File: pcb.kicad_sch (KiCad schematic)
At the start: 3 parts, among them SW1 SW_PUSH, U1 ProMicro

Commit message: rename repo and folder
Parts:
- added D10, D11, D12, D13, D14, D15, D16, D17, D18, D19, D2, D20, D21, D22, D23, D24, D25, D26, D27, D28, D29, D3, D30, D31, D32, D33, D34, D35, D36, D37, D38, D39, D4, D40, D41, D42, D5, D6, D7, D8, D9: 1N4148W, Diode_SMD:D_SOD-123, symbol Diode:1N4148W
- added SW10, SW11, SW12, SW13, SW14, SW15, SW16, SW17, SW18, SW2, SW20, SW21, SW22, SW23, SW24, SW25, SW26, SW27, SW28, SW29, SW3, SW30, SW31, SW32, SW33, SW34, SW35, SW36, SW37, SW38, SW39, SW4, SW40, SW41, SW42, SW43, SW5, SW6, SW7, SW8, SW9: SW_PUSH, symbol kbd:SW_PUSH
- added SW19: RESETSW, symbol kbd:SW_PUSH
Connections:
- net COL0: now also SW1.1, SW13.1, SW23.1, SW29.1, SW35.1, SW41.1, SW7.1
- net COL1: now also SW14.1, SW2.1, SW24.1, SW30.1, SW36.1, SW42.1, SW8.1
- net COL2: now also SW15.1, SW25.1, SW3.1, SW31.1, SW37.1, SW43.1, SW9.1
- net COL3: now also SW10.1, SW16.1, SW20.1, SW26.1, SW32.1, SW38.1, SW4.1
- net COL4: now also SW11.1, SW17.1, SW21.1, SW27.1, SW33.1, SW39.1, SW5.1
- net COL5: now also SW12.1, SW18.1, SW22.1, SW28.1, SW34.1, SW40.1, SW6.1
- net GND: now also SW19.2
- net ROW0: now also D1.1 (K), D2.1 (K), D3.1 (K), D4.1 (K), D5.1 (K), D6.1 (K)
- net ROW1: now also D10.1 (K), D11.1 (K), D12.1 (K), D7.1 (K), D8.1 (K), D9.1 (K)
- net ROW2: now also D13.1 (K), D14.1 (K), D15.1 (K), D16.1 (K), D17.1 (K), D18.1 (K)
- net ROW3: now also D19.1 (K), D20.1 (K), D21.1 (K)
- net ROW4: now also D22.1 (K), D23.1 (K), D24.1 (K), D25.1 (K), D26.1 (K), D27.1 (K)
- net ROW5: now also D28.1 (K), D29.1 (K), D30.1 (K), D31.1 (K), D32.1 (K), D33.1 (K)
- net ROW6: now also D34.1 (K), D35.1 (K), D36.1 (K), D37.1 (K), D38.1 (K), D39.1 (K)
- net ROW7: now also D40.1 (K), D41.1 (K), D42.1 (K)
- net at SW1.2: now also D1.2 (A)
- net at U1.22 (RST): now also SW19.1
- new net: D27.2 (A), SW28.2
- new net: D19.2 (A), SW20.2
- new net: D36.2 (A), SW37.2
- new net: D35.2 (A), SW36.2
- new net: D15.2 (A), SW15.2
- new net: D4.2 (A), SW4.2
- new net: D11.2 (A), SW11.2
- new net: D23.2 (A), SW24.2
- new net: D21.2 (A), SW22.2
- new net: D30.2 (A), SW31.2
- new net: D16.2 (A), SW16.2
- new net: D2.2 (A), SW2.2
- new net: D41.2 (A), SW42.2
- new net: D28.2 (A), SW29.2
- new net: D37.2 (A), SW38.2
- new net: D9.2 (A), SW9.2
- new net: D25.2 (A), SW26.2
- new net: D40.2 (A), SW41.2
- new net: D34.2 (A), SW35.2
- new net: D26.2 (A), SW27.2
- new net: D42.2 (A), SW43.2
- new net: D38.2 (A), SW39.2
- new net: D10.2 (A), SW10.2
- new net: D32.2 (A), SW33.2
- new net: D20.2 (A), SW21.2
- new net: D8.2 (A), SW8.2
- new net: D7.2 (A), SW7.2
- new net: D39.2 (A), SW40.2
- new net: D14.2 (A), SW14.2
- new net: D13.2 (A), SW13.2
- new net: D33.2 (A), SW34.2
- new net: D18.2 (A), SW18.2
- new net: D29.2 (A), SW30.2
- new net: D17.2 (A), SW17.2
- new net: D3.2 (A), SW3.2
- new net: D5.2 (A), SW5.2
- new net: D24.2 (A), SW25.2
- new net: D22.2 (A), SW23.2
- new net: D31.2 (A), SW32.2
- new net: D6.2 (A), SW6.2
- new net: D12.2 (A), SW12.2
- no-connect marks 0 -> 5
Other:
- moved on the sheet: D1, SW1

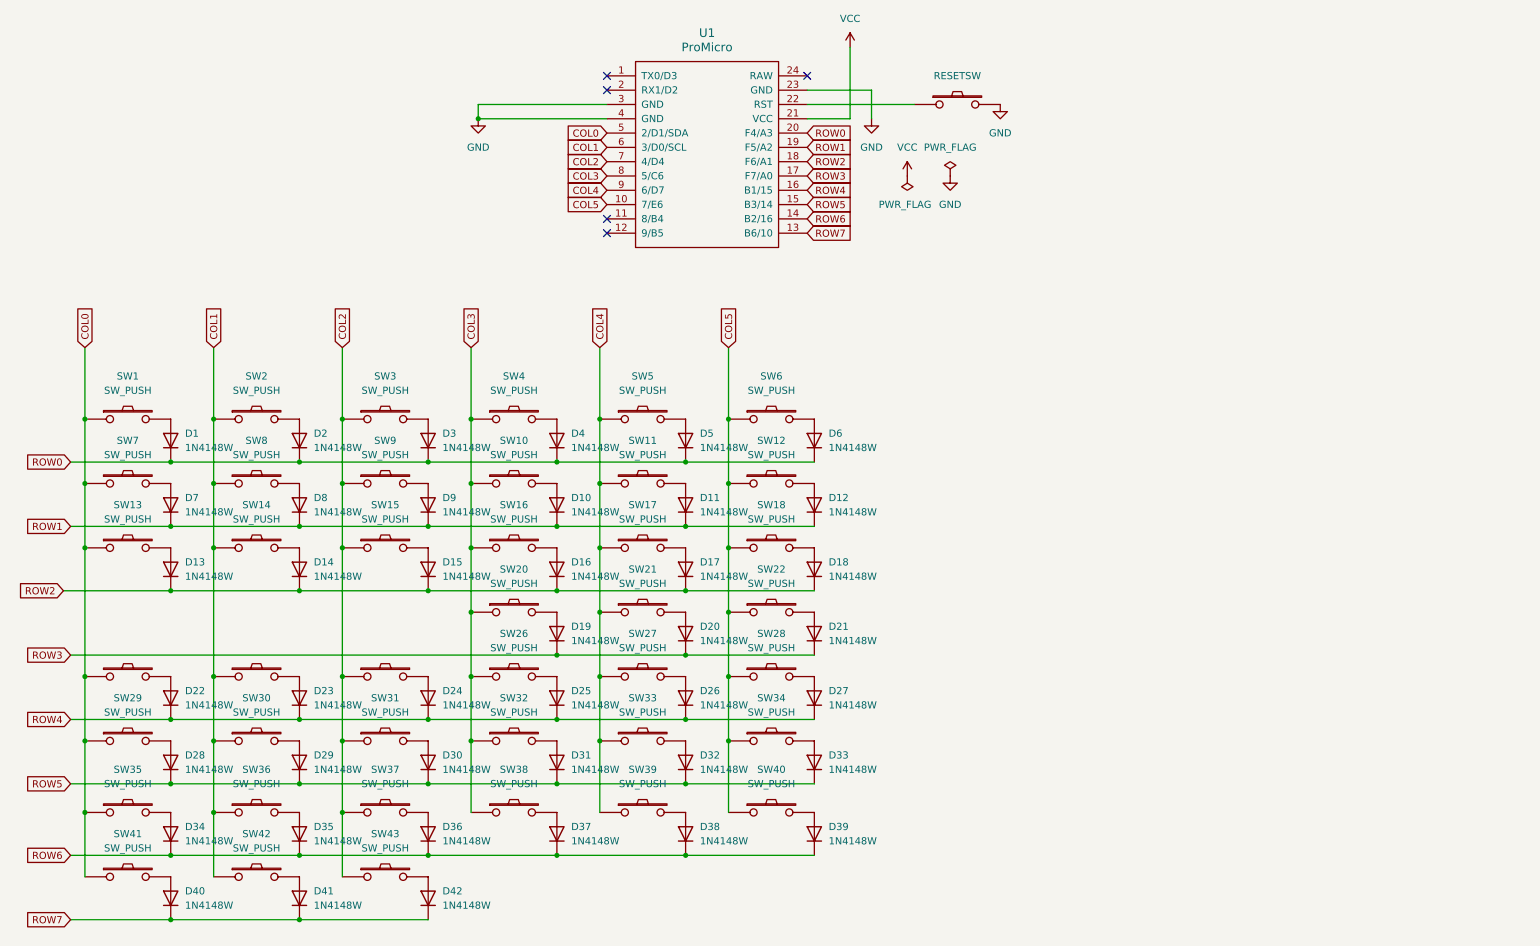
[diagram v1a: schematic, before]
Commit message: fixed switch numbering
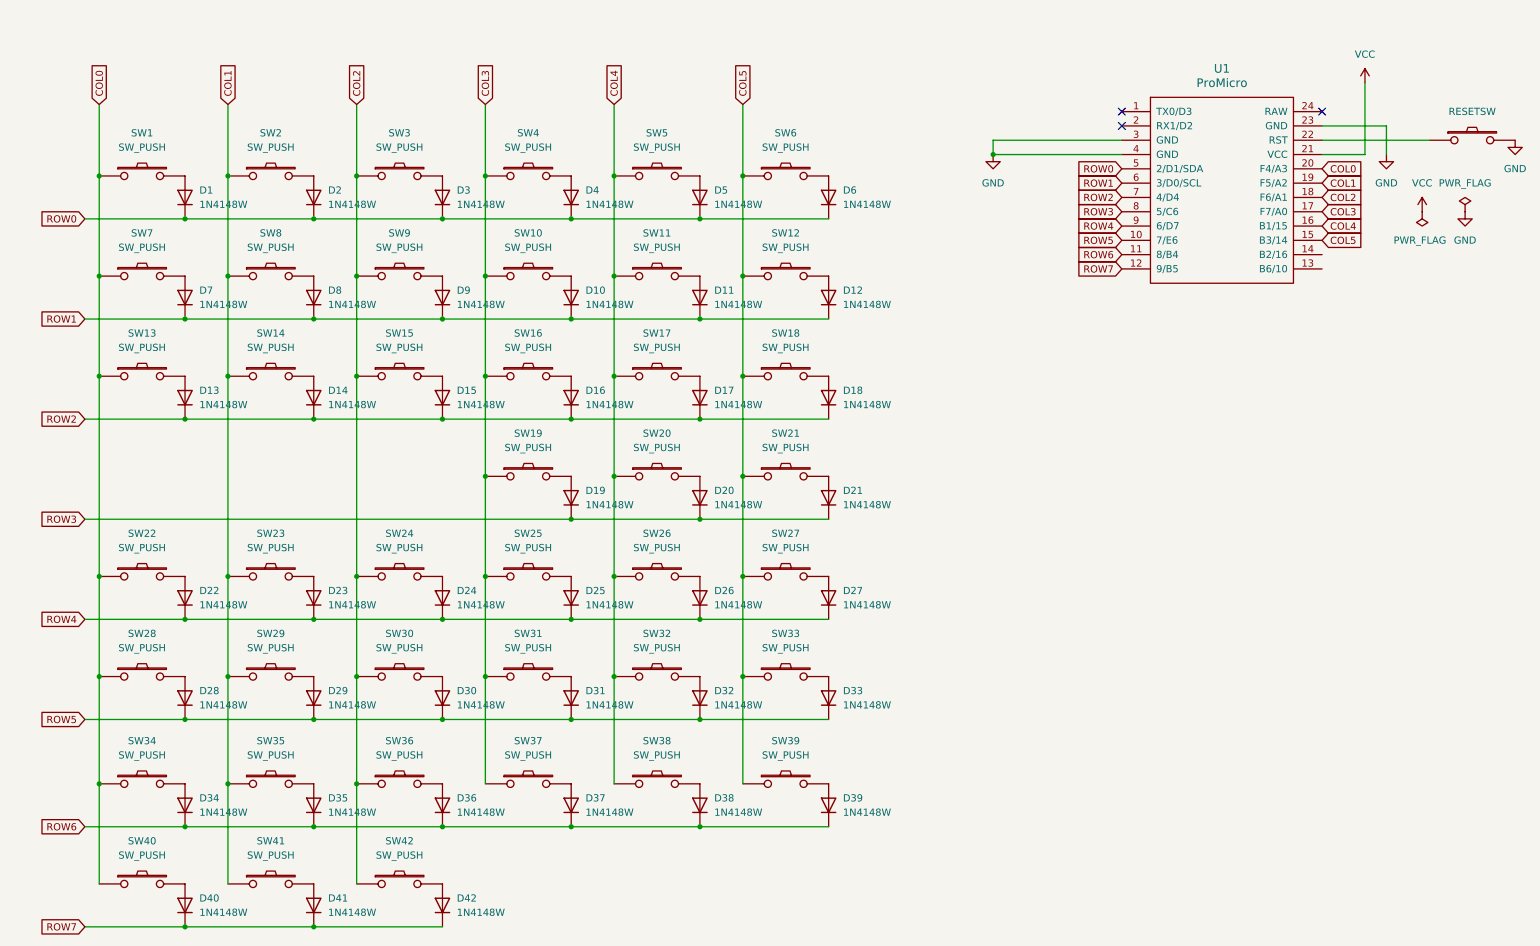
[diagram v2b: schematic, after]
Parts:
- renumbered SW19 to RSSW0, SW20 to SW19, SW21 to SW20, SW22 to SW21, SW23 to SW22, SW24 to SW23, SW25 to SW24, SW26 to SW25, SW27 to SW26, SW28 to SW27, SW29 to SW28, SW30 to SW29, SW31 to SW30, SW32 to SW31, SW33 to SW32, SW34 to SW33, SW35 to SW34, SW36 to SW35, SW37 to SW36, SW38 to SW37, SW39 to SW38, SW40 to SW39, SW41 to SW40, SW42 to SW41, SW43 to SW42
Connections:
- net COL0: now also U1.20 (F4/A3); no longer U1.5 (2/D1/SDA)
- net COL1: now also U1.19 (F5/A2); no longer U1.6 (3/D0/SCL)
- net COL2: now also U1.18 (F6/A1); no longer U1.7 (4/D4)
- net COL3: now also U1.17 (F7/A0); no longer U1.8 (5/C6)
- net COL4: now also U1.16 (B1/15); no longer U1.9 (6/D7)
- net COL5: now also U1.15 (B3/14); no longer U1.10 (7/E6)
- net ROW0: now also U1.5 (2/D1/SDA); no longer U1.20 (F4/A3)
- net ROW1: now also U1.6 (3/D0/SCL); no longer U1.19 (F5/A2)
- net ROW2: now also U1.7 (4/D4); no longer U1.18 (F6/A1)
- net ROW3: now also U1.8 (5/C6); no longer U1.17 (F7/A0)
- net ROW4: now also U1.9 (6/D7); no longer U1.16 (B1/15)
- net ROW5: now also U1.10 (7/E6); no longer U1.15 (B3/14)
- net ROW6: now also U1.11 (8/B4); no longer U1.14 (B2/16)
- net ROW7: now also U1.12 (9/B5); no longer U1.13 (B6/10)
- no-connect marks 5 -> 3
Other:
- moved on the sheet: D1, D10, D11, D12, D13, D14, D15, D16, D17, D18, D19, D2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

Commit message: assigned footprint
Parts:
- D1, D10, D11, D12, D13, D14, D15, D16, D17, D18, D19, D2, D20, D21, D22, D23, D24, D25, D26, D27, D28, D29, D3, D30, D31, D32, D33, D34, D35, D36, D37, D38, D39, D4, D40, D41, D42, D5, D6, D7, D8, D9: footprint Diode_SMD:D_SOD-123 -> kbd:D3_TH_SMD_v2
- RSSW0: footprint (none) -> kbd:ResetSW_1side
- SW1, SW10, SW11, SW12, SW13, SW14, SW15, SW16, SW17, SW18, SW19, SW2, SW20, SW21, SW22, SW23, SW24, SW25, SW26, SW27, SW28, SW29, SW3, SW30, SW31, SW32, SW33, SW34, SW35, SW36, SW37, SW38, SW39, SW4, SW40, SW41, SW42, SW5, SW6, SW7, SW8, SW9: footprint (none) -> kbd:CherryMX_Hotswap
- U1: footprint (none) -> kbd:ProMicro_v3.5
